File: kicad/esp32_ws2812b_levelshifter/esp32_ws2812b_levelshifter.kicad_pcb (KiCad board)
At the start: 2 copper layers, 50 x 35 mm, 0 parts

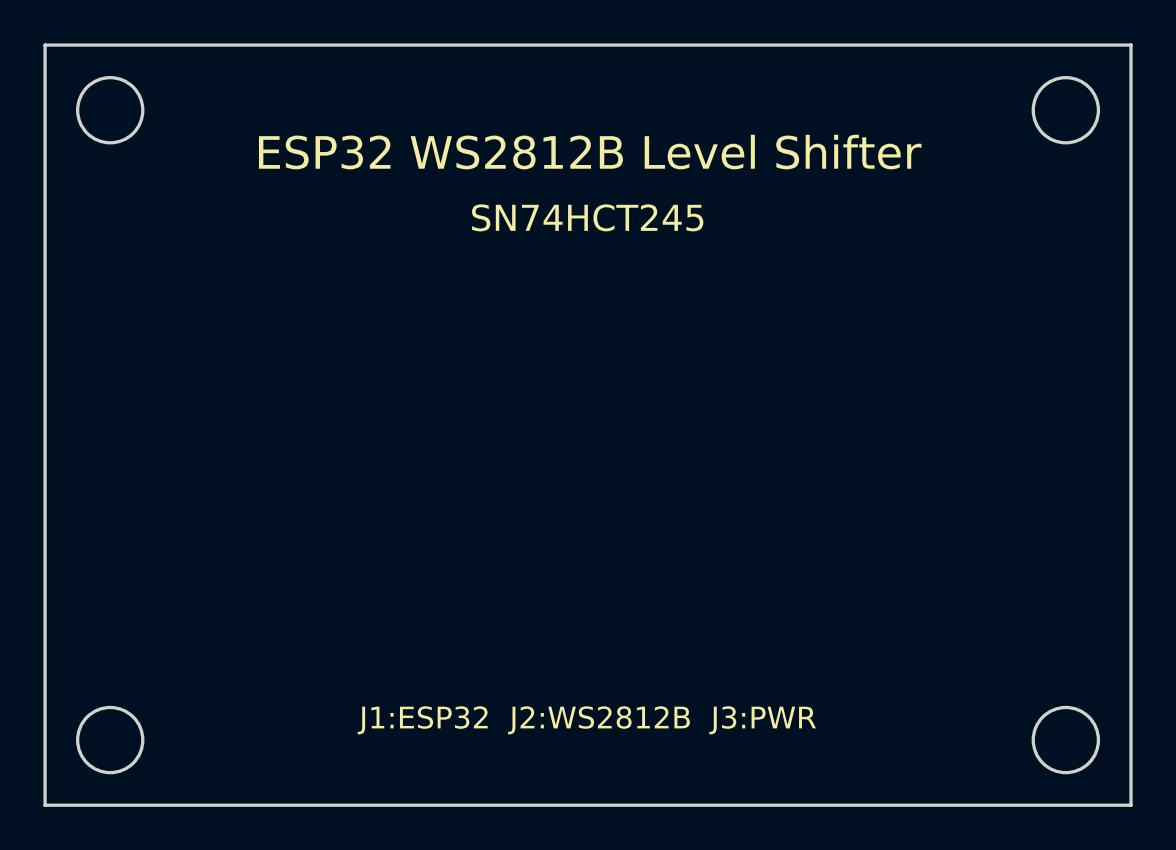
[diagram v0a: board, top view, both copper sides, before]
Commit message: refactor: update to SN74HCT125 (DIP-14) per user schematic
- Replace SN74HCT245 (DIP-20) with SN74HCT125 (DIP-14, quad buffer)
- All ~OE pins tied to GND (outputs always enabled)
- Channel 1: GPIO13 -> 1A (pin2) -> 1Y (pin3) -> R1 -> WS2812B DIN
- Resistor changed from 330R to 62-100R per reference schematic
- 100nF bypass cap between VCC (pin14) and GND (pin7)
- PCB reduced to 40x30mm (smaller IC footprint)
- Updated BOM and documentation

Co-Authored-By: josefrizi@gmail.com <josefrizi@gmail.com>
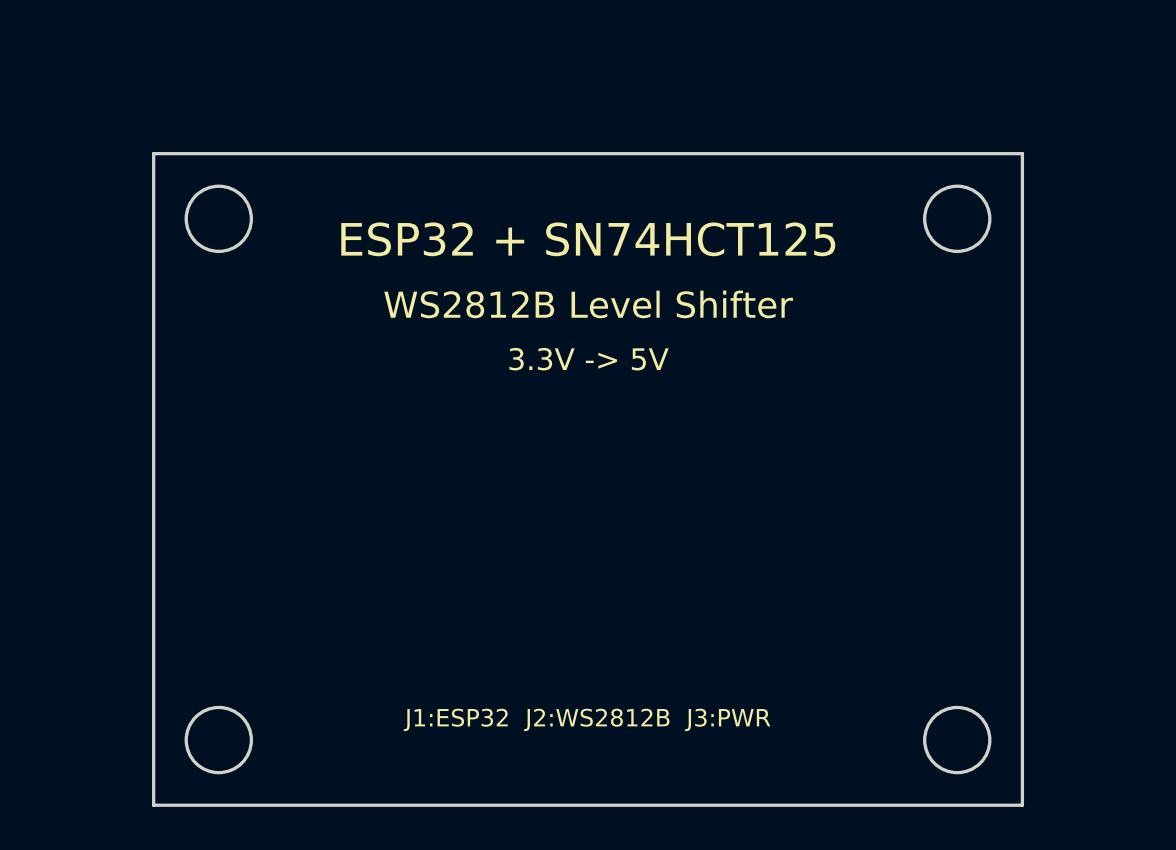
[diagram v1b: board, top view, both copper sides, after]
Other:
- board size 50 x 35 mm -> 40 x 30 mm
- board text added: "3.3V -> 5V"
- board text added: "ESP32 + SN74HCT125"
- board text added: "WS2812B Level Shifter"
- board text removed: "ESP32 WS2812B Level Shifter"
- board text removed: "SN74HCT245"
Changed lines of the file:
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@@
   (paper "A4")
   (title_block
-    (title "ESP32 + SN74HCT245 Level Shifter para WS2812B")
+    (title "ESP32 + SN74HCT125 Level Shifter para WS2812B")
     (date "2026-05-03")
-    (rev "1.0")
+    (rev "2.0")
     (company "ESP32 Radio Bluetooth")
   )
@@
     (48 "B.Fab" user "B.Fabrication")
     (49 "F.Fab" user "F.Fabrication")
-    (50 "User.1" user)
-    (51 "User.2" user)
-    (52 "User.3" user)
-    (53 "User.4" user)
-    (54 "User.5" user)
-    (55 "User.6" user)
-    (56 "User.7" user)
-    (57 "User.8" user)
-    (58 "User.9" user)
   )
   (setup
     (stackup
-      (layer "F.SilkS"
-        (type "Top Silk Screen")
-      )
-      (layer "F.Paste"
-        (type "Top Solder Paste")
-      )
-      (layer "F.Mask"
-        (type "Top Solder Mask")
-        (thickness 0.01)
-      )
-      (layer "F.Cu"
-        (type "copper")
-        (thickness 0.035)
-      )
-      (layer "dielectric 1"
-        (type "core")
-        (thickness 1.51)
-        (material "FR4")
-        (epsilon_r 4.5)
-        (loss_tangent 0.02)
-      )
-      (layer "B.Cu"
-        (type "copper")
-        (thickness 0.035)
-      )
-      (layer "B.Mask"
-        (type "Bottom Solder Mask")
-        (thickness 0.01)
-      )
-      (layer "B.Paste"
-        (type "Bottom Solder Paste")
-      )
-      (layer "B.SilkS"
-        (type "Bottom Silk Screen")
-      )
+      (layer "F.SilkS" (type "Top Silk Screen"))
+      (layer "F.Paste" (type "Top Solder Paste"))
+      (layer "F.Mask" (type "Top Solder Mask") (thickness 0.01))
+      (layer "F.Cu" (type "copper") (thickness 0.035))
+      (layer "dielectric 1" (type "core") (thickness 1.51) (material "FR4") (epsilon_r 4.5) (loss_tangent 0.02))
+      (layer "B.Cu" (type "copper") (thickness 0.035))
+      (layer "B.Mask" (type "Bottom Solder Mask") (thickness 0.01))
+      (layer "B.Paste" (type "Bottom Solder Paste"))
+      (layer "B.SilkS" (type "Bottom Silk Screen"))
       (copper_finish "None")
       (dielectric_constraints no)
@@
       (usegerberadvancedattributes yes)
       (creategerberjobfile yes)
-      (dashed_line_dash_ratio 12.000000)
-      (dashed_line_gap_ratio 3.000000)
       (svgprecision 4)
       (plotframeref no)
@@
       (hpglpenspeed 20)
       (hpglpendiameter 15.000000)
-      (pdf_front_fp_property_popups yes)
-      (pdf_back_fp_property_popups yes)
       (dxfpolygonmode yes)
       (dxfimperialunits yes)
@@
   (net 4 "WS2812B_DIN")
   (net 5 "+3V3")
-  (net 6 "Net-(U1-A2)")
-  (net 7 "Net-(U1-A3)")
-  (net 8 "Net-(U1-A4)")
-  (net 9 "Net-(U1-A5)")
-  (net 10 "Net-(U1-A6)")
-  (net 11 "Net-(U1-A7)")
-  (net 12 "Net-(U1-A8)")
-  (net 13 "Net-(U1-B2)")
-  (net 14 "Net-(U1-B3)")
-  (net 15 "Net-(U1-B4)")
-  (net 16 "Net-(U1-B5)")
-  (net 17 "Net-(U1-B6)")
-  (net 18 "Net-(U1-B7)")
-  (net 19 "Net-(U1-B8)")
-  ;; Board outline - 50mm x 35mm
+  ;; Board outline - 40mm x 30mm (smaller board for DIP-14)
   (gr_rect
-    (start 95 60)
-    (end 145 95)
-    (stroke
-      (width 0.15)
-      (type default)
-    )
+    (start 100 65)
+    (end 140 95)
+    (stroke (width 0.15) (type default))
     (fill none)
     (layer "Edge.Cuts")
   )
-  ;; Title text on silkscreen
-  (gr_text "ESP32 WS2812B Level Shifter"
-    (at 120 65)
+  ;; Silkscreen labels
+  (gr_text "ESP32 + SN74HCT125"
+    (at 120 69)
     (layer "F.SilkS")
-    (effects
-      (font
-        (size 1.5 1.5)
-        (thickness 0.15)
-      )
-    )
+    (effects (font (size 1.5 1.5) (thickness 0.15)))
   )
-  (gr_text "SN74HCT245"
-    (at 120 68)
+  (gr_text "WS2812B Level Shifter"
+    (at 120 72)
     (layer "F.SilkS")
-    (effects
-      (font
-        (size 1.2 1.2)
-        (thickness 0.12)
-      )
-    )
+    (effects (font (size 1.2 1.2) (thickness 0.12)))
+  )
+  (gr_text "3.3V -> 5V"
+    (at 120 74.5)
+    (layer "F.SilkS")
+    (effects (font (size 1 1) (thickness 0.1)))
   )
   (gr_text "J1:ESP32  J2:WS2812B  J3:PWR"
     (at 120 91)
     (layer "F.SilkS")
-    (effects
-      (font
-        (size 1 1)
-        (thickness 0.1)
-      )
-    )
+    (effects (font (size 0.8 0.8) (thickness 0.08)))
   )
-  ;; Mounting holes corners
+  ;; Mounting holes (M3)
   (gr_circle
-    (center 98 63)
-    (end 99.5 63)
-    (stroke
-      (width 0.15)
-      (type default)
-    )
-    (fill none)
-    (layer "Edge.Cuts")
+    (center 103 68) (end 104.5 68)
+    (stroke (width 0.15) (type default)) (fill none) (layer "Edge.Cuts")
   )
   (gr_circle
-    (center 142 63)
-    (end 143.5 63)
-    (stroke
-      (width 0.15)
-      (type default)
-    )
-    (fill none)
-    (layer "Edge.Cuts")
+    (center 137 68) (end 138.5 68)
+    (stroke (width 0.15) (type default)) (fill none) (layer "Edge.Cuts")
   )
   (gr_circle
-    (center 98 92)
-    (end 99.5 92)
-    (stroke
-      (width 0.15)
-      (type default)
-    )
-    (fill none)
-    (layer "Edge.Cuts")
+    (center 103 92) (end 104.5 92)
+    (stroke (width 0.15) (type default)) (fill none) (layer "Edge.Cuts")
   )
   (gr_circle
-    (center 142 92)
-    (end 143.5 92)
-    (stroke
-      (width 0.15)
-      (type default)
-    )
-    (fill none)
-    (layer "Edge.Cuts")
+    (center 137 92) (end 138.5 92)
+    (stroke (width 0.15) (type default)) (fill none) (layer "Edge.Cuts")
   )
 )
